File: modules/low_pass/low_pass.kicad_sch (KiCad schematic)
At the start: 33 parts, among them U1 MCP6002-xSN, U2 VTL5C, U3 MCP6002-xSN, U4 VTL5C, U5 VTL5C, U7 MCP6002-xSN

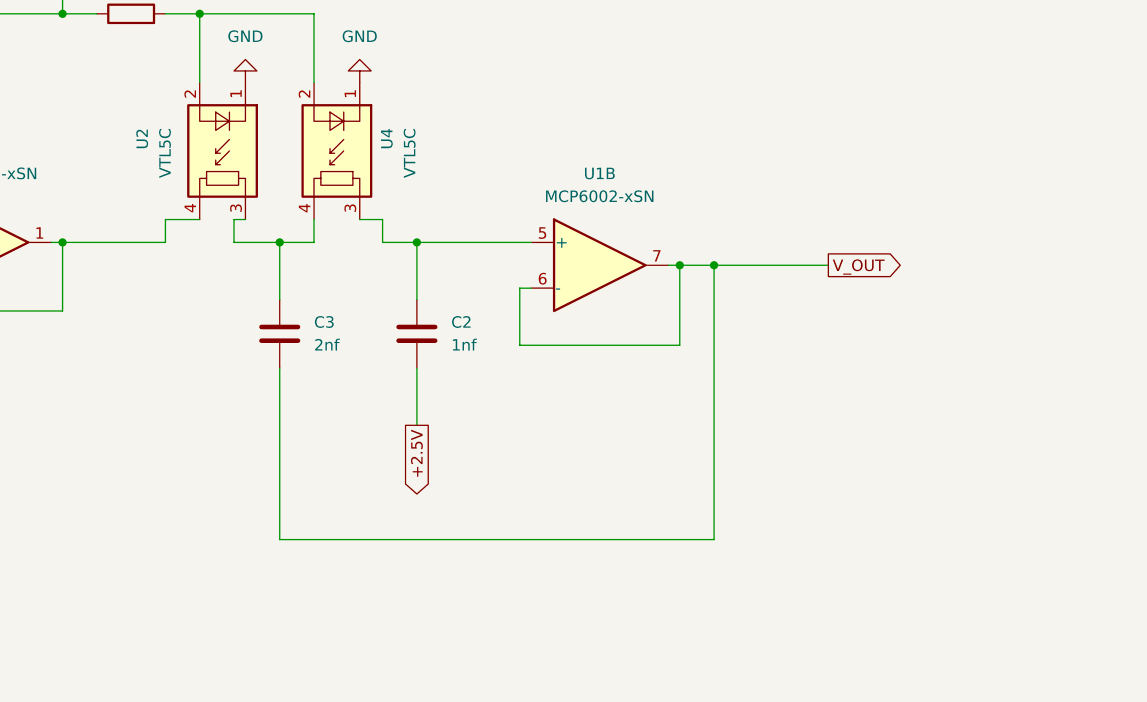
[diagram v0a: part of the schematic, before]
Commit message: Add Sallen Key capacitors with commonly available caps
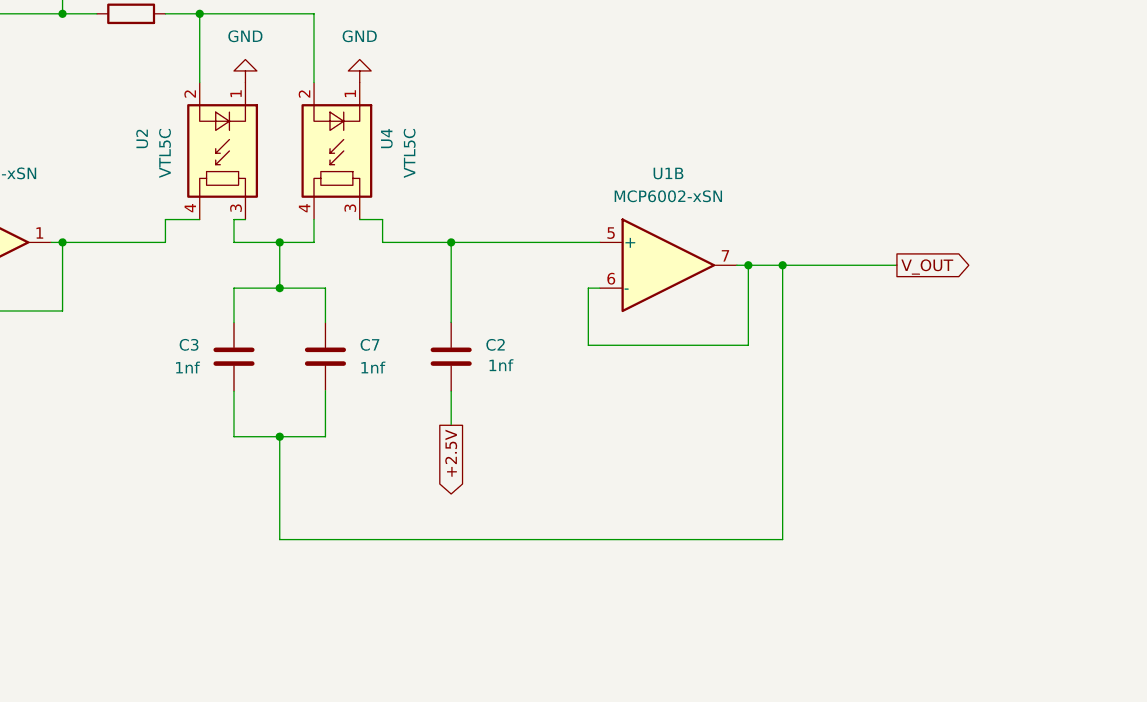
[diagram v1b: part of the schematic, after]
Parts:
- added C7: 1nf, symbol Device:C
- C3: value 2nf -> 1nf
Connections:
- net V_OUT: now also C7.2
- net at C3.1, U2.3, U4.4: now also C7.1
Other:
- moved on the sheet: C2, C3, U1B

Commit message: Making the schematic ready for PCB
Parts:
- C1: footprint (none) -> Capacitor_SMD:C_0402_1005Metric
- C2: renamed from C4; footprint (none) -> Capacitor_SMD:C_0402_1005Metric
- C3: renamed from C5; footprint (none) -> Capacitor_SMD:C_0402_1005Metric
- C4: renamed from C3; footprint (none) -> Capacitor_SMD:C_0402_1005Metric
- C5: renamed from C7; footprint (none) -> Capacitor_SMD:C_0402_1005Metric
- C6: renamed from C2; footprint (none) -> Capacitor_SMD:C_0402_1005Metric
- C7: renamed from C6; footprint (none) -> Capacitor_SMD:C_0402_1005Metric
- D1: footprint (none) -> LED_SMD:LED_0603_1608Metric
- R1: renamed from R8; footprint (none) -> Resistor_SMD:R_0402_1005Metric
- R10, R11: footprint (none) -> Resistor_SMD:R_0402_1005Metric
- R2: renamed from R5; footprint (none) -> Resistor_SMD:R_0402_1005Metric
- R3: renamed from R7; footprint (none) -> Resistor_SMD:R_0402_1005Metric
- R4: renamed from R6; footprint (none) -> Resistor_SMD:R_0402_1005Metric
- R5: renamed from R1; footprint (none) -> Resistor_SMD:R_0402_1005Metric
- R6: renamed from R2; footprint (none) -> Resistor_SMD:R_0402_1005Metric
- R7: renamed from R4; footprint (none) -> Resistor_SMD:R_0402_1005Metric
- R8: renamed from R9; footprint (none) -> Resistor_SMD:R_0402_1005Metric
- R9: renamed from R3; footprint (none) -> Resistor_SMD:R_0402_1005Metric
- RV1, RV2: footprint (none) -> BreadModular_Pots:Potentiometer_RV09
- U1: renamed from U3; footprint (none) -> Package_SO:SOIC-8-1EP_3.9x4.9mm_P1.27mm_EP2.29x3mm
- U2: renamed from U5; footprint OptoDevice:PerkinElmer_VTL5C -> BreadModular_MISC:VTL5C
- U3: renamed from U1; footprint (none) -> Package_SO:SOIC-8-1EP_3.9x4.9mm_P1.27mm_EP2.29x3mm
- U4: renamed from U7; footprint (none) -> Package_SO:SOIC-8-1EP_3.9x4.9mm_P1.27mm_EP2.29x3mm
- U5: renamed from U2; footprint OptoDevice:PerkinElmer_VTL5C -> BreadModular_MISC:VTL5C
- U6: renamed from U4; footprint OptoDevice:PerkinElmer_VTL5C -> BreadModular_MISC:VTL5C
- renumbered OUTPUT2 to OUTPUT1
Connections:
- net V_OUT is gone; now on net AUDIO_OUT: C4.2, C5.2, U3.6 (-), U3.7
- net AUDIO_IN: now also INPUT1.1 (Pin_1)
- net CUTOFF_CV_IN: now also INPUT1.3 (Pin_3)
- net MOD_CV_IN: now also INPUT1.2 (Pin_2)
- net AUDIO_OUT: now reaches OUTPUT1.1 (Pin_1)
- net AUDIO_OUT: now also OUTPUT1.2 (Pin_2), OUTPUT1.3 (Pin_3), OUTPUT1.4 (Pin_4), OUTPUT1.5 (Pin_5)
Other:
- moved on the sheet: C3, OUTPUT1, U4C

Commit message: Finalized the design
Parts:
- removed R8: 51k, Resistor_SMD:R_0402_1005Metric, symbol Device:R
- added R9: 1k, Resistor_SMD:R_0402_1005Metric, symbol Device:R
- added V4: 0, symbol Simulation_SPICE:VDC
- R11: footprint Resistor_SMD:R_0402_1005Metric -> Resistor_SMD:R_1206_3216Metric
- R8: renamed from R9; footprint Resistor_SMD:R_0402_1005Metric -> Resistor_SMD:R_1206_3216Metric
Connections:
- net AUDIO_OUT: now also R9.2; no longer C4.2, C5.2, U3.6 (-), U3.7
- net CUTOFF_CV_IN: now also V4.1
- net GND: now also V4.2
- net at U2.2 (+): now also R7.2
- new net: C4.2, C5.2, R9.1, U3.6 (-), U3.7
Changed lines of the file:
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@@
 	(wire
 		(pts
-			(xy 55.88 101.6) (xy 57.15 101.6)
-		)
-		(stroke
-			(width 0)
-			(type default)
-		)
-	)
-	(wire
-		(pts
 			(xy 87.63 265.43) (xy 66.04 265.43)
 		)
@@
 	(wire
 		(pts
-			(xy 142.24 163.83) (xy 154.94 163.83)
+			(xy 142.24 163.83) (xy 152.4 163.83)
 		)
 		(stroke
@@
 	(wire
 		(pts
+			(xy 160.02 163.83) (xy 167.64 163.83)
+		)
+		(stroke
+			(width 0)
+			(type default)
+		)
+	)
+	(wire
+		(pts
 			(xy 102.87 57.15) (xy 102.87 43.18)
 		)
@@
 	(wire
 		(pts
-			(xy 48.26 101.6) (xy 45.72 101.6)
+			(xy 45.72 101.6) (xy 57.15 101.6)
 		)
 		(stroke
@@
 		)
 	)
+	(global_label "CUTOFF_CV_IN"
+		(shape input)
+		(at 391.16 220.98 90)
+		(fields_autoplaced yes)
+		(effects
+			(font
+				(size 1.27 1.27)
+			)
+			(justify left)
+		)
+		(property "Intersheetrefs" "${INTERSHEET_REFS}"
+			(at 391.16 204.6899 90)
+			(effects
+				(font
+					(size 1.27 1.27)
+				)
+				(justify left)
+				(hide yes)
+			)
+		)
+	)
 	(global_label "+2.5V"
 		(shape output)
@@
 	(global_label "AUDIO_OUT"
 		(shape output)
-		(at 154.94 163.83 0)
+		(at 167.64 163.83 0)
 		(fields_autoplaced yes)
 		(effects
@@
 		)
 		(property "Intersheetrefs" "${INTERSHEET_REFS}"
-			(at 168.1458 163.83 0)
+			(at 180.8458 163.83 0)
 			(effects
 				(font
@@
 	)
 	(symbol
+		(lib_id "Device:R")
+		(at 156.21 163.83 90)
+		(unit 1)
+		(exclude_from_sim no)
+		(in_bom yes)
+		(on_board yes)
+		(dnp no)
+		(fields_autoplaced yes)
+		(property "Reference" "R9"
+			(at 156.21 157.48 90)
+			(effects
+				(font
+					(size 1.27 1.27)
+				)
+			)
+		)
+		(property "Value" "1k"
+			(at 156.21 160.02 90)
+			(effects
+				(font
+					(size 1.27 1.27)
+				)
+			)
+		)
+		(property "Footprint" "Resistor_SMD:R_0402_1005Metric"
+			(at 156.21 165.608 90)
+			(effects
+				(font
+					(size 1.27 1.27)
+				)
+				(hide yes)
+			)
+		)
+		(property "Datasheet" "~"
+			(at 156.21 163.83 0)
+			(effects
+				(font
+					(size 1.27 1.27)
+				)
+				(hide yes)
+			)
+		)
+		(property "Description" "Resistor"
+			(at 156.21 163.83 0)
+			(effects
+				(font
+					(size 1.27 1.27)
+				)
+				(hide yes)
+			)
+		)
+		(pin "1"
+		)
+		(pin "2"
+		)
+		(instances
+			(project "low_pass"
+				(path "/b63493d3-5f6d-47e3-845b-87e7090fc1ab"
+					(reference "R9")
+					(unit 1)
+				)
+			)
+		)
+	)
+	(symbol
 		(lib_id "power:GND")
 		(at 317.5 127 0)
@@
 			)
 		)
-		(property "Sim.Params" "pos=0.5"
+		(property "Sim.Params" "pos=0.9"
 			(at 30.48 57.15 90)
 			(effects
@@
 		(dnp no)
 		(fields_autoplaced yes)
-		(property "Reference" "R9"
+		(property "Reference" "R8"
 			(at 69.85 129.54 90)
 			(effects
@@
 			)
 		)
-		(property "Footprint" "Resistor_SMD:R_0402_1005Metric"
+		(property "Footprint" "Resistor_SMD:R_1206_3216Metric"
 			(at 69.85 137.668 90)
 			(effects
@@
 			(project "low_pass"
 				(path "/b63493d3-5f6d-47e3-845b-87e7090fc1ab"
-					(reference "R9")
+					(reference "R8")
 					(unit 1)
 				)
@@
 	)
 	(symbol
+		(lib_id "power:GND")
+		(at 391.16 231.14 0)
+		(unit 1)
+		(exclude_from_sim no)
+		(in_bom yes)
+		(on_board yes)
+		(dnp no)
+		(property "Reference" "#PWR020"
+			(at 391.16 237.49 0)
+			(effects
+				(font
+					(size 1.27 1.27)
+				)
+				(hide yes)
+			)
+		)
+		(property "Value" "GND"
+			(at 391.16 236.22 0)
+			(effects
+				(font
+					(size 1.27 1.27)
+				)
+			)
+		)
+		(property "Footprint" ""
+			(at 391.16 231.14 0)
+			(effects
+				(font
+					(size 1.27 1.27)
+				)
+				(hide yes)
+			)
+		)
+		(property "Datasheet" ""
+			(at 391.16 231.14 0)
+			(effects
+				(font
+					(size 1.27 1.27)
+				)
+				(hide yes)
+			)
+		)
+		(property "Description" "Power symbol creates a global label with name \"GND\" , ground"
+			(at 391.16 231.14 0)
+			(effects
+				(font
+					(size 1.27 1.27)
+				)
+				(hide yes)
+			)
+		)
+		(pin "1"
+		)
+		(instances
+			(project "low_pass"
+				(path "/b63493d3-5f6d-47e3-845b-87e7090fc1ab"
+					(reference "#PWR020")
+					(unit 1)
+				)
+			)
+		)
+	)
+	(symbol
 		(lib_id "Device:R")
 		(at 106.68 252.73 90)
@@
 			)
 		)
-		(property "Footprint" "Resistor_SMD:R_0402_1005Metric"
+		(property "Footprint" "Resistor_SMD:R_1206_3216Metric"
 			(at 106.68 254.508 90)
 			(effects
@@
 	)
 	(symbol
-		(lib_id "Device:R")
-		(at 52.07 101.6 90)
+		(lib_id "Simulation_SPICE:VDC")
+		(at 391.16 226.06 0)
 		(unit 1)
 		(exclude_from_sim no)
 		(in_bom yes)
-		(on_board yes)
+		(on_board no)
 		(dnp no)
-		(fields_autoplaced yes)
-		(property "Reference" "R8"
-			(at 52.07 95.25 90)
+		(property "Reference" "V4"
+			(at 394.97 224.6601 0)
 			(effects
 				(font
 					(size 1.27 1.27)
 				)
+				(justify left)
 			)
 		)
-		(property "Value" "51k"
-			(at 52.07 97.79 90)
+		(property "Value" "0"
+			(at 394.97 227.2001 0)
 			(effects
 				(font
 					(size 1.27 1.27)
 				)
+				(justify left)
 			)
 		)
-		(property "Footprint" "Resistor_SMD:R_0402_1005Metric"
-			(at 52.07 103.378 90)
+		(property "Footprint" ""
+			(at 391.16 226.06 0)
 			(effects
 				(font
@@
 			)
 		)
-		(property "Datasheet" "~"
-			(at 52.07 101.6 0)
+		(property "Datasheet" "https://ngspice.sourceforge.io/docs/ngspice-html-manual/manual.xhtml#sec_Independent_Sources_for"
+			(at 391.16 226.06 0)
 			(effects
 				(font
@@
 			)
 		)
-		(property "Description" "Resistor"
-			(at 52.07 101.6 0)
+		(property "Description" "Voltage source, DC"
+			(at 391.16 226.06 0)
 			(effects
 				(font
@@
 			)
 		)
+		(property "Sim.Pins" "1=+ 2=-"
+			(at 391.16 226.06 0)
+			(effects
+				(font
+					(size 1.27 1.27)
+				)
+				(hide yes)
+			)
+		)
+		(property "Sim.Type" "DC"
+			(at 391.16 226.06 0)
+			(effects
+				(font
+					(size 1.27 1.27)
+				)
+				(hide yes)
+			)
+		)
+		(property "Sim.Device" "V"
+			(at 391.16 226.06 0)
+			(effects
+				(font
+					(size 1.27 1.27)
+				)
+				(justify left)
+				(hide yes)
+			)
+		)
 		(pin "1"
 		)
@@
 			(project "low_pass"
 				(path "/b63493d3-5f6d-47e3-845b-87e7090fc1ab"
-					(reference "R8")
+					(reference "V4")
 					(unit 1)
 				)

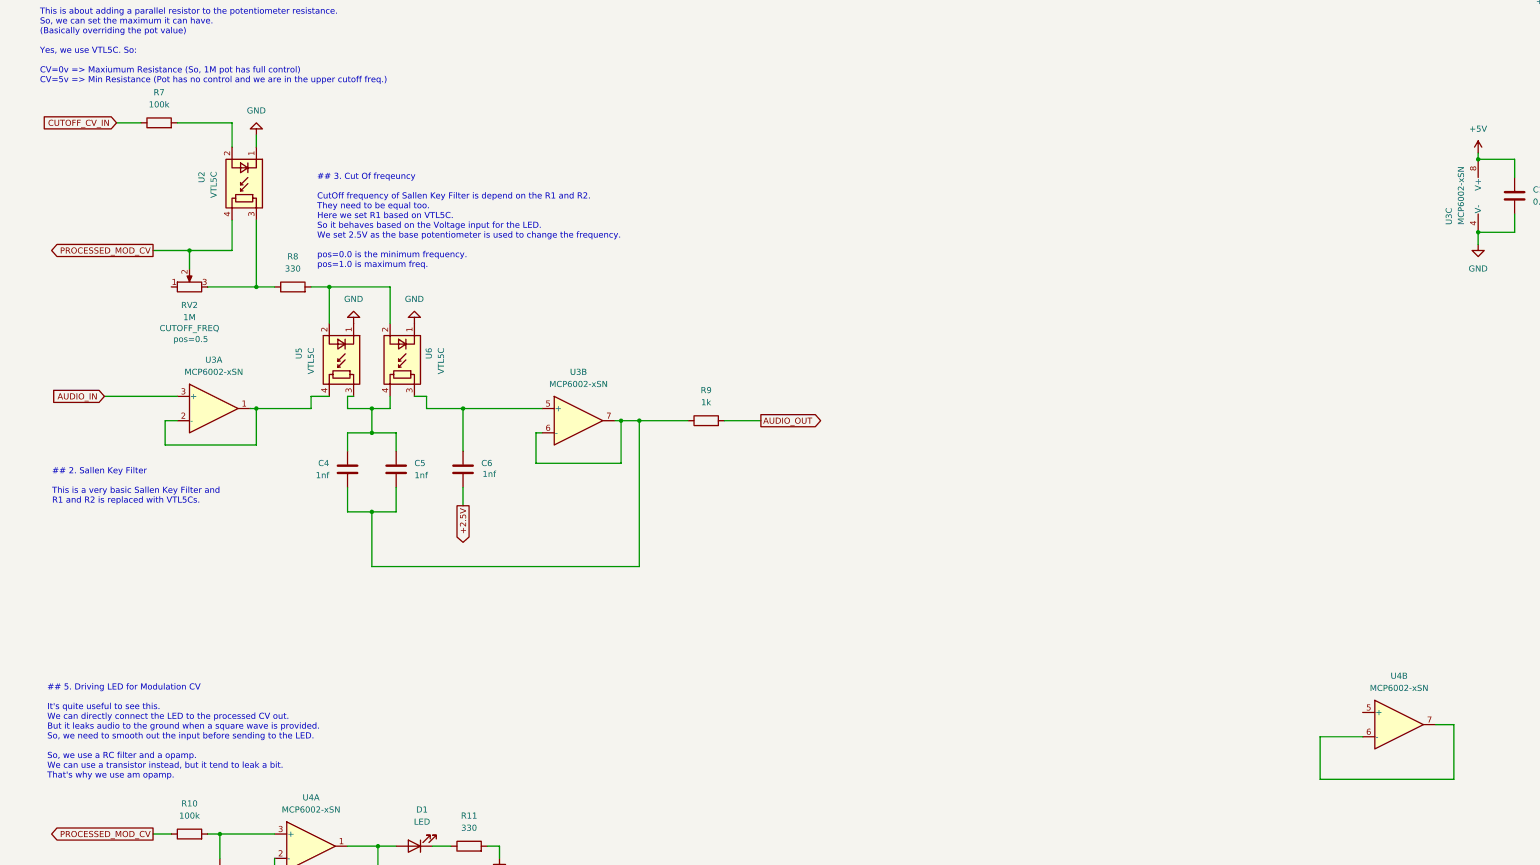
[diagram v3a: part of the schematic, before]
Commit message: layout components in the PCB
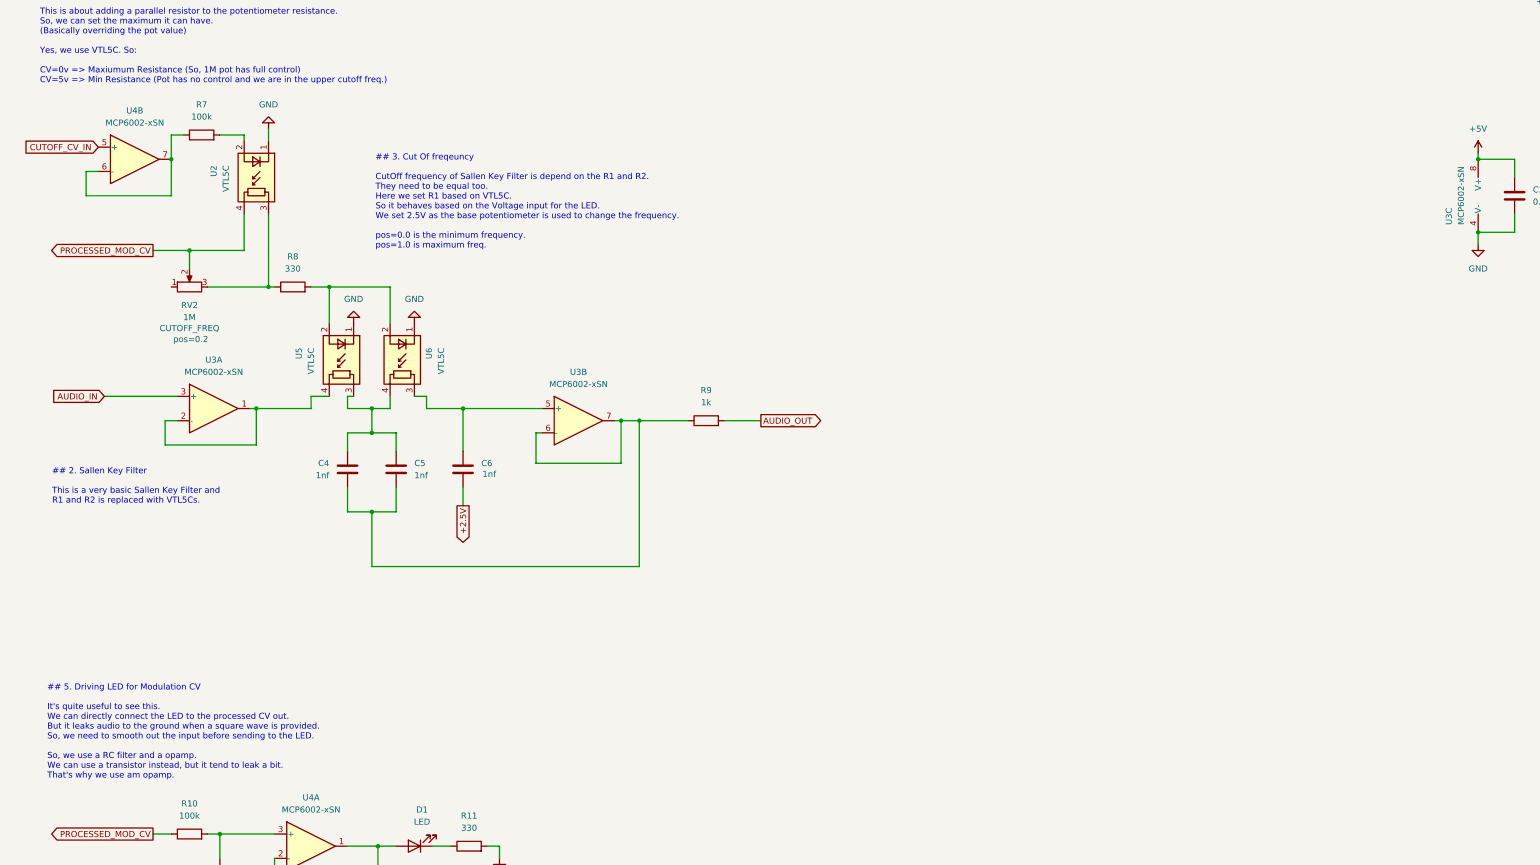
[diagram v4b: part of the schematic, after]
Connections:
- net CUTOFF_CV_IN: now also U4.5 (+); no longer R7.1
- net at U4.6 (-), U4.7: now also R7.1
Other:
- moved on the sheet: R7, U2, U4B

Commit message: Finalized low_pass
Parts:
- R11, R8: footprint Resistor_SMD:R_1206_3216Metric -> Resistor_SMD:R_0805_2012Metric
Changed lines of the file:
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@@
 			)
 		)
-		(property "Footprint" "Resistor_SMD:R_1206_3216Metric"
+		(property "Footprint" "Resistor_SMD:R_0805_2012Metric"
 			(at 69.85 137.668 90)
 			(effects
@@
 			)
 		)
-		(property "Footprint" "Resistor_SMD:R_1206_3216Metric"
+		(property "Footprint" "Resistor_SMD:R_0805_2012Metric"
 			(at 106.68 254.508 90)
 			(effects
